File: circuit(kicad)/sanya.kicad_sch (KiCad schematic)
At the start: 10 parts, among them J1 Oled, J2 Micro_SD_Card, J3 AVR-ISP-6, SW1 Up, SW2 Down, SW3 Set, SW4 SW_DPDT_x2, U1 ATmega328P-A

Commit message: sshnk1
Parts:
- removed J3: AVR-ISP-6, Connector_IDC:IDC-Header_2x03_P2.54mm_Vertical, symbol Connector:AVR-ISP-6
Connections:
- net Earth: now also SW4.2 (B); no longer BT1.2 (-)
- net RST: now also SW4.3 (C)
- net VCC: now also BT1.1 (+); no longer SW4.2 (B)
- net at SW4.1 (A): now also BT1.2 (-); no longer BT1.1 (+)
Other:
- moved on the sheet: BT1
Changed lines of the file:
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@@
+    (stroke (width 0) (type default))
+  )
+  (wire (pts (xy 73.66 46.99) (xy 71.12 46.99))
     (stroke (width 0) (type default))
   )
@@
     (stroke (width 0) (type default))
   )
-  (wire (pts (xy 71.12 46.99) (xy 74.93 46.99))
+  (wire (pts (xy 58.42 52.07) (xy 58.42 54.61))
     (stroke (width 0) (type default))
   )
@@
     (stroke (width 0) (type default))
   )
-  (label "MOSI" (at 85.09 125.73 0) (fields_autoplaced)
-    (effects (font (size 1.27 1.27)) (justify left bottom))
-  )
   (label "PD5" (at 152.4 58.42 180) (fields_autoplaced)
     (effects (font (size 1.27 1.27)) (justify right bottom))
@@
     (effects (font (size 1.27 1.27)) (justify right bottom))
   )
-  (label "SCK" (at 85.09 128.27 0) (fields_autoplaced)
-    (effects (font (size 1.27 1.27)) (justify left bottom))
-  )
   (label "PD4" (at 152.4 64.77 180) (fields_autoplaced)
     (effects (font (size 1.27 1.27)) (justify right bottom))
@@
     (effects (font (size 1.27 1.27)) (justify left bottom))
   )
-  (label "MISO" (at 85.09 123.19 0) (fields_autoplaced)
+  (label "RST" (at 58.42 54.61 0) (fields_autoplaced)
     (effects (font (size 1.27 1.27)) (justify left bottom))
   )
@@
     (effects (font (size 1.27 1.27)) (justify left bottom))
   )
-  (label "RST" (at 85.09 130.81 0) (fields_autoplaced)
-    (effects (font (size 1.27 1.27)) (justify left bottom))
-  )
   (label "PD6" (at 152.4 50.8 180) (fields_autoplaced)
     (effects (font (size 1.27 1.27)) (justify right bottom))
@@
   )
   (label "PB2" (at 124.46 46.99 0) (fields_autoplaced)
+    (effects (font (size 1.27 1.27)) (justify left bottom))
+  )
+  (label "VCC" (at 73.66 46.99 0) (fields_autoplaced)
     (effects (font (size 1.27 1.27)) (justify left bottom))
   )
@@
         (path "/d61570fb-d04c-4d77-a695-b08b64c70a6b"
           (reference "#PWR07") (unit 1)
-        )
-      )
-    )
-  )
-  (symbol (lib_id "Connector:AVR-ISP-6") (at 74.93 128.27 0) (unit 1)
-    (in_bom yes) (on_board yes) (dnp no) (fields_autoplaced)
-    (property "Reference" "J3" (at 66.04 126.365 0)
-      (effects (font (size 1.27 1.27)) (justify right))
-    )
-    (property "Value" "AVR-ISP-6" (at 66.04 128.905 0)
-      (effects (font (size 1.27 1.27)) (justify right))
-    )
-    (property "Footprint" "Connector_IDC:IDC-Header_2x03_P2.54mm_Vertical" (at 68.58 127 90)
-      (effects (font (size 1.27 1.27)) hide)
-    )
-    (property "Datasheet" " ~" (at 42.545 142.24 0)
-      (effects (font (size 1.27 1.27)) hide)
-    )
-    (pin "1")
-    (pin "2")
-    (pin "3")
-    (pin "4")
-    (pin "5")
-    (pin "6")
-    (instances
-      (project "sanya"
-        (path "/d61570fb-d04c-4d77-a695-b08b64c70a6b"
-          (reference "J3") (unit 1)
         )
       )
@@
     )
   )
-  (symbol (lib_id "power:Earth") (at 74.93 46.99 0) (unit 1)
-    (in_bom yes) (on_board yes) (dnp no) (fields_autoplaced)
-    (property "Reference" "#PWR02" (at 74.93 53.34 0)
-      (effects (font (size 1.27 1.27)) hide)
-    )
-    (property "Value" "Earth" (at 74.93 50.8 0)
-      (effects (font (size 1.27 1.27)) hide)
-    )
-    (property "Footprint" "" (at 74.93 46.99 0)
-      (effects (font (size 1.27 1.27)) hide)
-    )
-    (property "Datasheet" "~" (at 74.93 46.99 0)
+  (symbol (lib_id "power:Earth") (at 35.56 49.53 180) (unit 1)
+    (in_bom yes) (on_board yes) (dnp no) (fields_autoplaced)
+    (property "Reference" "#PWR02" (at 35.56 43.18 0)
+      (effects (font (size 1.27 1.27)) hide)
+    )
+    (property "Value" "Earth" (at 35.56 45.72 0)
+      (effects (font (size 1.27 1.27)) hide)
+    )
+    (property "Footprint" "" (at 35.56 49.53 0)
+      (effects (font (size 1.27 1.27)) hide)
+    )
+    (property "Datasheet" "~" (at 35.56 49.53 0)
       (effects (font (size 1.27 1.27)) hide)
     )
@@
     )
   )
-  (symbol (lib_id "power:VCC") (at 72.39 115.57 0) (unit 1)
-    (in_bom yes) (on_board yes) (dnp no) (fields_autoplaced)
-    (property "Reference" "#PWR04" (at 72.39 119.38 0)
-      (effects (font (size 1.27 1.27)) hide)
-    )
-    (property "Value" "VCC" (at 72.39 111.76 0)
-      (effects (font (size 1.27 1.27)))
-    )
-    (property "Footprint" "" (at 72.39 115.57 0)
-      (effects (font (size 1.27 1.27)) hide)
-    )
-    (property "Datasheet" "" (at 72.39 115.57 0)
-      (effects (font (size 1.27 1.27)) hide)
-    )
-    (pin "1")
-    (instances
-      (project "sanya"
-        (path "/d61570fb-d04c-4d77-a695-b08b64c70a6b"
-          (reference "#PWR04") (unit 1)
-        )
-      )
-    )
-  )
-  (symbol (lib_id "Device:Battery") (at 66.04 46.99 90) (unit 1)
-    (in_bom yes) (on_board yes) (dnp no) (fields_autoplaced)
-    (property "Reference" "BT1" (at 65.659 40.64 90)
-      (effects (font (size 1.27 1.27)))
-    )
-    (property "Value" "Battery" (at 65.659 43.18 90)
-      (effects (font (size 1.27 1.27)))
-    )
-    (property "Footprint" "Battery:BatteryHolder_Keystone_3000_1x12mm" (at 64.516 46.99 90)
-      (effects (font (size 1.27 1.27)) hide)
-    )
-    (property "Datasheet" "~" (at 64.516 46.99 90)
+  (symbol (lib_id "Device:Battery") (at 66.04 46.99 270) (unit 1)
+    (in_bom yes) (on_board yes) (dnp no) (fields_autoplaced)
+    (property "Reference" "BT1" (at 66.421 40.64 90)
+      (effects (font (size 1.27 1.27)))
+    )
+    (property "Value" "Battery" (at 66.421 43.18 90)
+      (effects (font (size 1.27 1.27)))
+    )
+    (property "Footprint" "Battery:BatteryHolder_Keystone_3000_1x12mm" (at 67.564 46.99 90)
+      (effects (font (size 1.27 1.27)) hide)
+    )
+    (property "Datasheet" "~" (at 67.564 46.99 90)
       (effects (font (size 1.27 1.27)) hide)
     )
@@
         )
       )
-    )
-  )
-  (symbol (lib_id "power:Earth") (at 72.39 138.43 0) (unit 1)
-    (in_bom yes) (on_board yes) (dnp no) (fields_autoplaced)
-    (property "Reference" "#PWR05" (at 72.39 144.78 0)
-      (effects (font (size 1.27 1.27)) hide)
-    )
-    (property "Value" "Earth" (at 72.39 142.24 0)
-      (effects (font (size 1.27 1.27)) hide)
-    )
-    (property "Footprint" "" (at 72.39 138.43 0)
-      (effects (font (size 1.27 1.27)) hide)
-    )
-    (property "Datasheet" "~" (at 72.39 138.43 0)
-      (effects (font (size 1.27 1.27)) hide)
-    )
-    (pin "1")
-    (instances
-      (project "sanya"
-        (path "/d61570fb-d04c-4d77-a695-b08b64c70a6b"
-          (reference "#PWR05") (unit 1)
-        )
-      )
-    )
-  )
-  (symbol (lib_id "power:VCC") (at 35.56 49.53 0) (unit 1)
-    (in_bom yes) (on_board yes) (dnp no) (fields_autoplaced)
-    (property "Reference" "#PWR01" (at 35.56 53.34 0)
-      (effects (font (size 1.27 1.27)) hide)
-    )
-    (property "Value" "VCC" (at 35.56 45.72 0)
-      (effects (font (size 1.27 1.27)))
-    )
-    (property "Footprint" "" (at 35.56 49.53 0)
-      (effects (font (size 1.27 1.27)) hide)
-    )
-    (property "Datasheet" "" (at 35.56 49.53 0)
-      (effects (font (size 1.27 1.27)) hide)
-    )
-    (pin "1")
-    (instances
-      (project "sanya"
-        (path "/d61570fb-d04c-4d77-a695-b08b64c70a6b"
-          (reference "#PWR01") (unit 1)
-        )
-      )

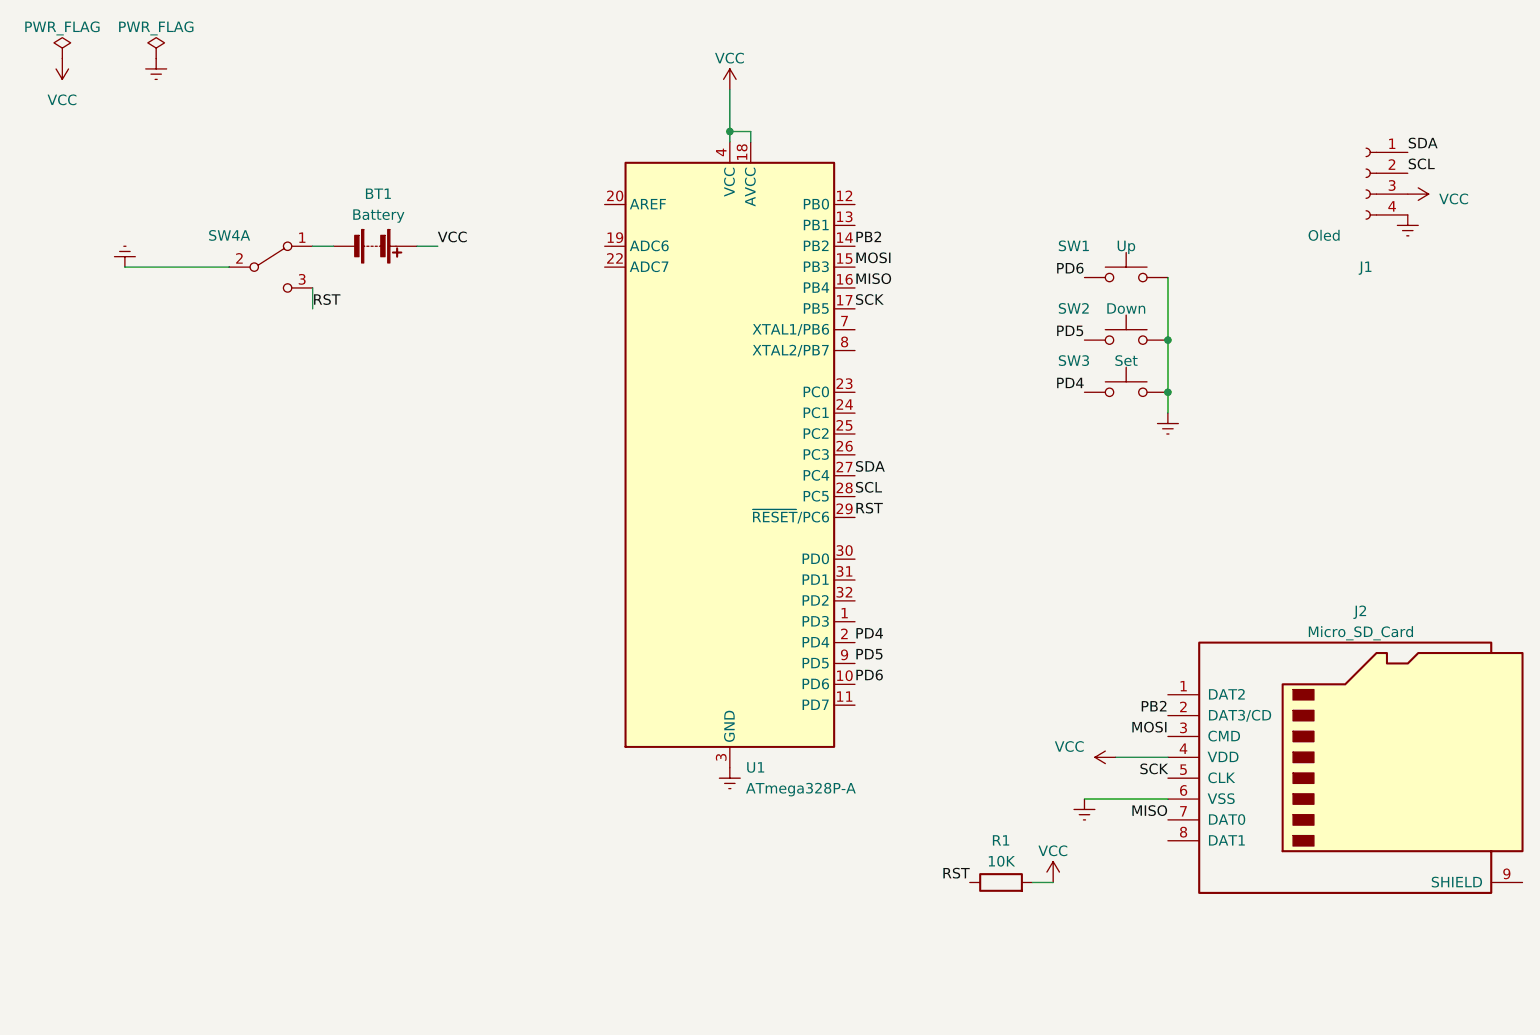
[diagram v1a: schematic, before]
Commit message: Подкорректировал посадочные места, провел дорожки автотрассировщиком (еще не финальный вариант)
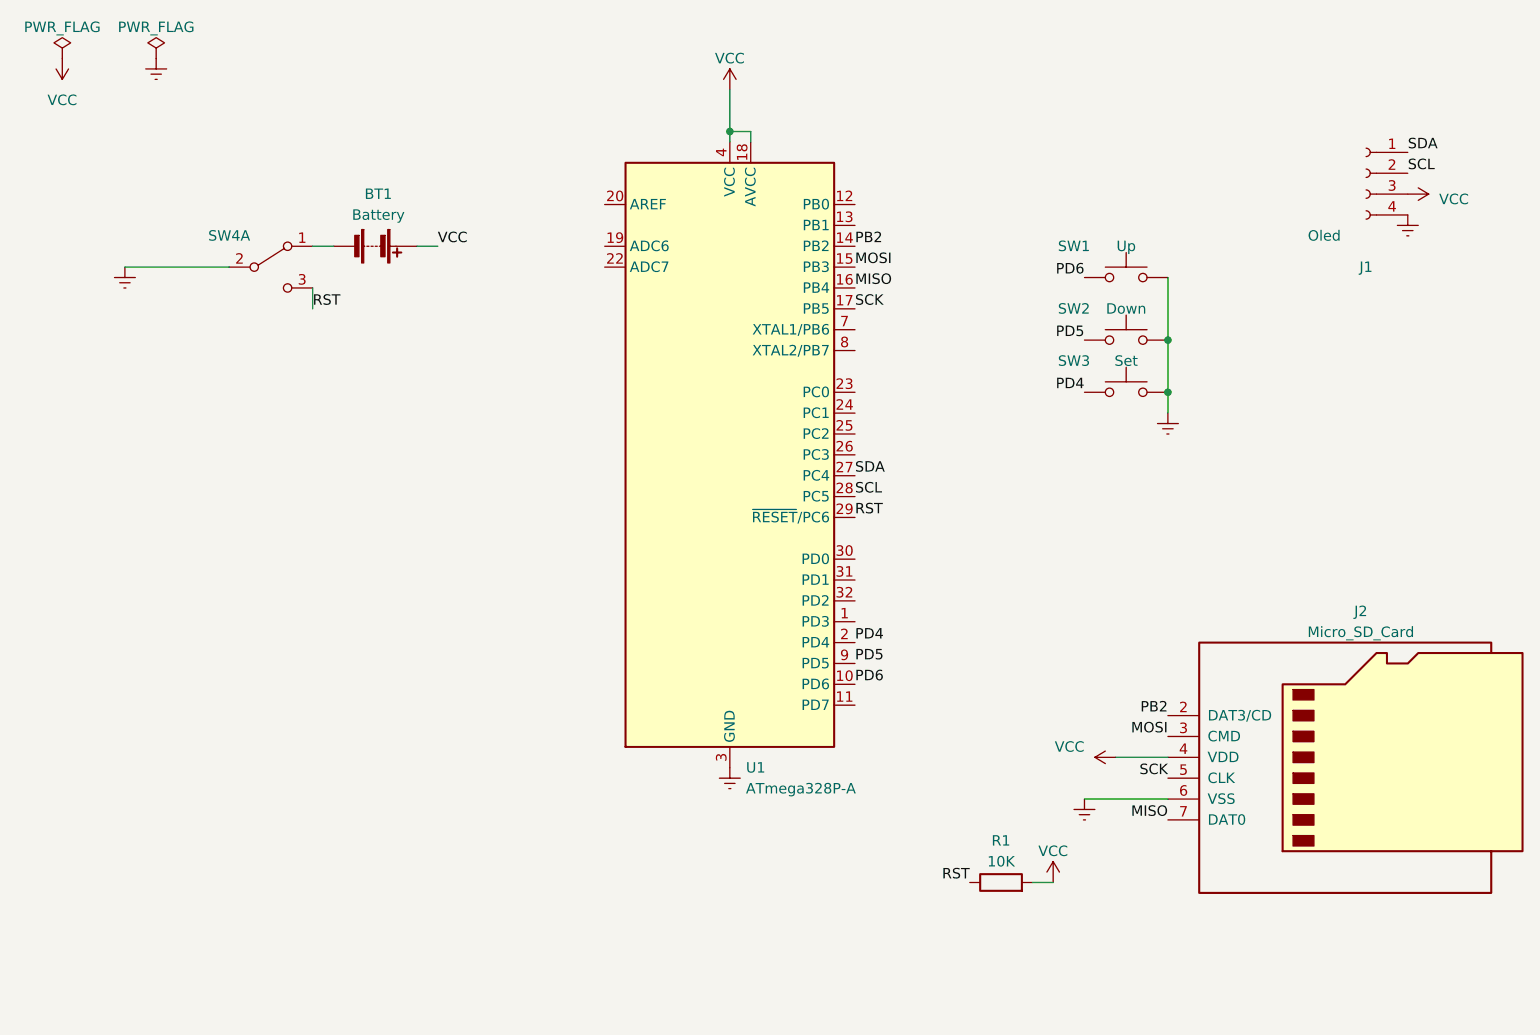
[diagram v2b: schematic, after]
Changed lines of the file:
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@@
       (effects (font (size 1.27 1.27)) hide)
     )
-    (pin "1")
     (pin "2")
     (pin "3")
@@
     (pin "6")
     (pin "7")
-    (pin "8")
-    (pin "9")
     (instances
       (project "sanya"
@@
     )
   )
-  (symbol (lib_id "power:Earth") (at 35.56 49.53 180) (unit 1)
+  (symbol (lib_id "power:Earth") (at 35.56 49.53 0) (unit 1)
     (in_bom yes) (on_board yes) (dnp no) (fields_autoplaced)
-    (property "Reference" "#PWR02" (at 35.56 43.18 0)
+    (property "Reference" "#PWR02" (at 35.56 55.88 0)
       (effects (font (size 1.27 1.27)) hide)
     )
-    (property "Value" "Earth" (at 35.56 45.72 0)
+    (property "Value" "Earth" (at 35.56 53.34 0)
       (effects (font (size 1.27 1.27)) hide)
     )

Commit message: Изменил посадочное место для батарейки; Заново протрассировал дорожки
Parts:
- BT1: footprint Battery:BatteryHolder_Keystone_3000_1x12mm -> Library:CR2032_BatteryHolder
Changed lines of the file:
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@@
       (effects (font (size 1.27 1.27)))
     )
-    (property "Footprint" "Battery:BatteryHolder_Keystone_3000_1x12mm" (at 67.564 46.99 90)
+    (property "Footprint" "Library:CR2032_BatteryHolder" (at 67.564 46.99 90)
       (effects (font (size 1.27 1.27)) hide)
     )

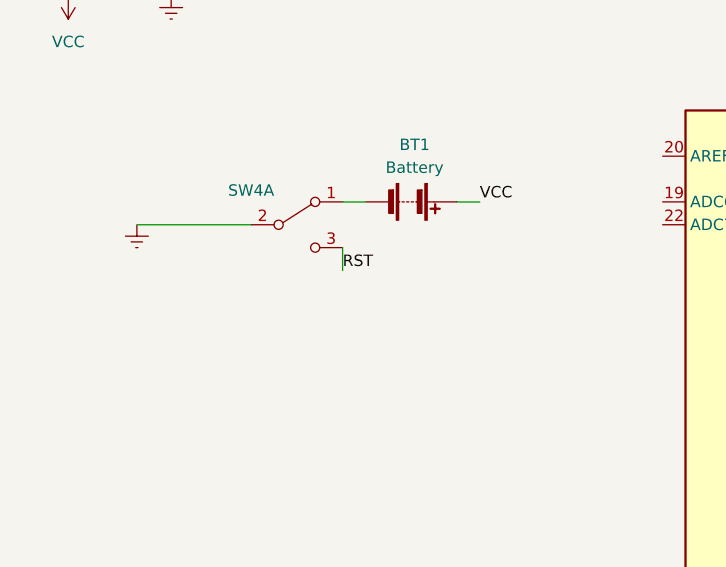
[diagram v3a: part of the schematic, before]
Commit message: Сделал перемычку м/у RST и GND
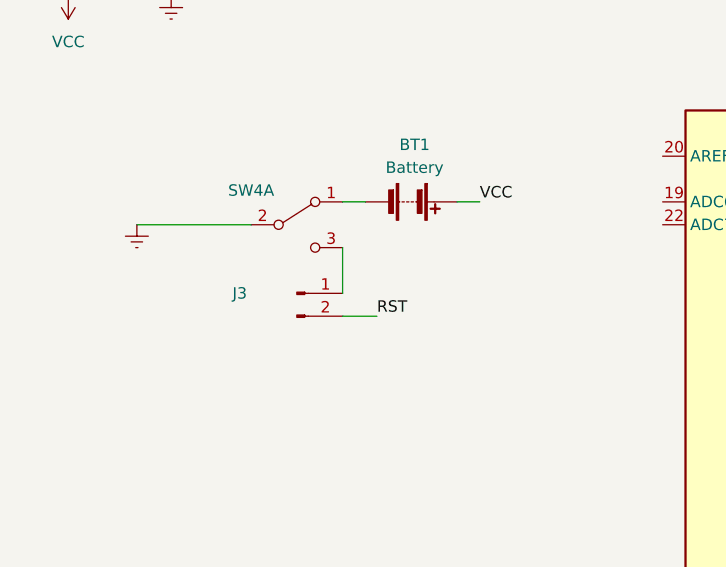
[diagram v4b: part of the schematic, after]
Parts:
- added J3: sw1, Connector_PinHeader_2.54mm:PinHeader_1x02_P2.54mm_Vertical, symbol Connector:Conn_01x02_Pin
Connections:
- net RST: now also J3.2 (Pin_2); no longer SW4.3 (C)
- new net: J3.1 (Pin_1), SW4.3 (C)
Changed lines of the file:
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@@
   (junction (at 109.22 33.02) (diameter 0) (color 0 0 0 0)
   )
+  (wire (pts (xy 58.42 59.69) (xy 62.23 59.69))
+    (stroke (width 0) (type default))
+  )
   (wire (pts (xy 146.05 124.46) (xy 148.59 124.46))
     (stroke (width 0) (type default))
@@
     (stroke (width 0) (type default))
   )
-  (wire (pts (xy 58.42 52.07) (xy 58.42 54.61))
+  (wire (pts (xy 58.42 52.07) (xy 58.42 57.15))
     (stroke (width 0) (type default))
   )
@@
     (effects (font (size 1.27 1.27)) (justify left bottom))
   )
-  (label "RST" (at 58.42 54.61 0) (fields_autoplaced)
+  (label "RST" (at 62.23 59.69 0) (fields_autoplaced)
     (effects (font (size 1.27 1.27)) (justify left bottom))
   )
@@
         )
       )
+    )
+  )
+  (symbol (lib_id "Connector:Conn_01x02_Pin") (at 53.34 57.15 0) (unit 1)
+    (in_bom yes) (on_board yes) (dnp no)
+    (property "Reference" "J3" (at 46.99 57.15 0)
+      (effects (font (size 1.27 1.27)))
+    )
+    (property "Value" "sw1" (at 53.975 54.61 0)
+      (effects (font (size 1.27 1.27)) hide)
+    )
+    (property "Footprint" "Connector_PinHeader_2.54mm:PinHeader_1x02_P2.54mm_Vertical" (at 53.34 57.15 0)
+      (effects (font (size 1.27 1.27)) hide)
+    )
+    (property "Datasheet" "~" (at 53.34 57.15 0)
+      (effects (font (size 1.27 1.27)) hide)
+    )
+    (pin "1")
+    (pin "2")
+    (instances
+      (project "sanya"
+        (path "/d61570fb-d04c-4d77-a695-b08b64c70a6b"
+          (reference "J3") (unit 1)
+        )
+      )
